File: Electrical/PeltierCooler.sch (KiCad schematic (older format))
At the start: 45 parts

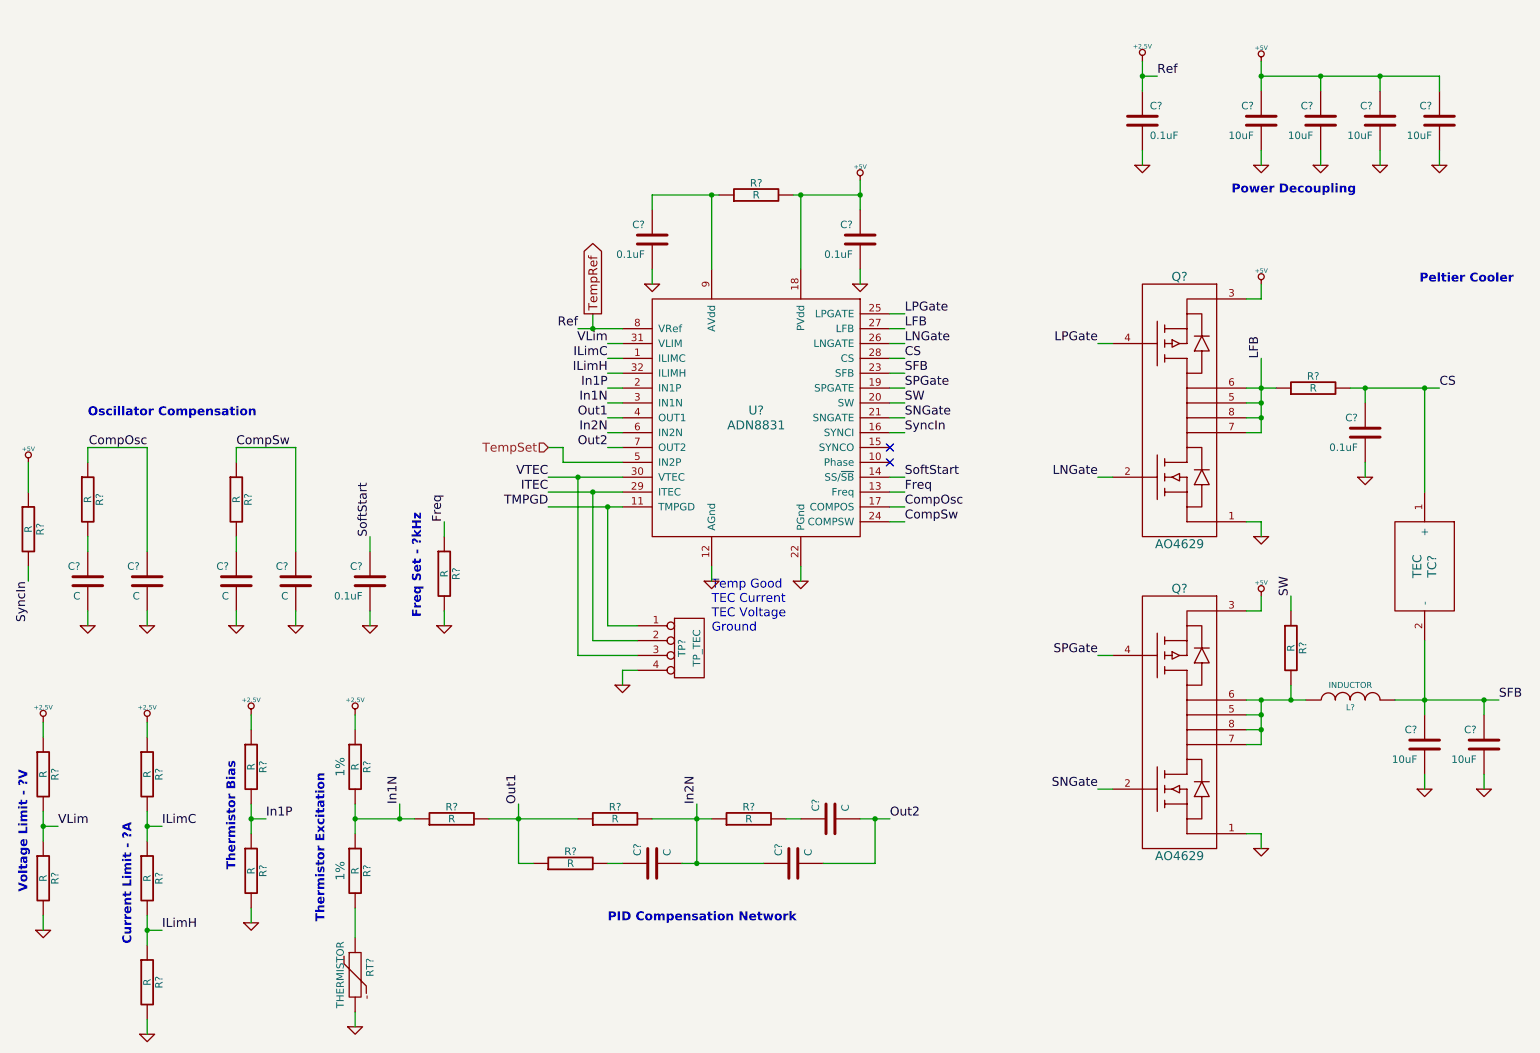
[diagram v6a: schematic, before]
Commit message: Implementing TEC controller
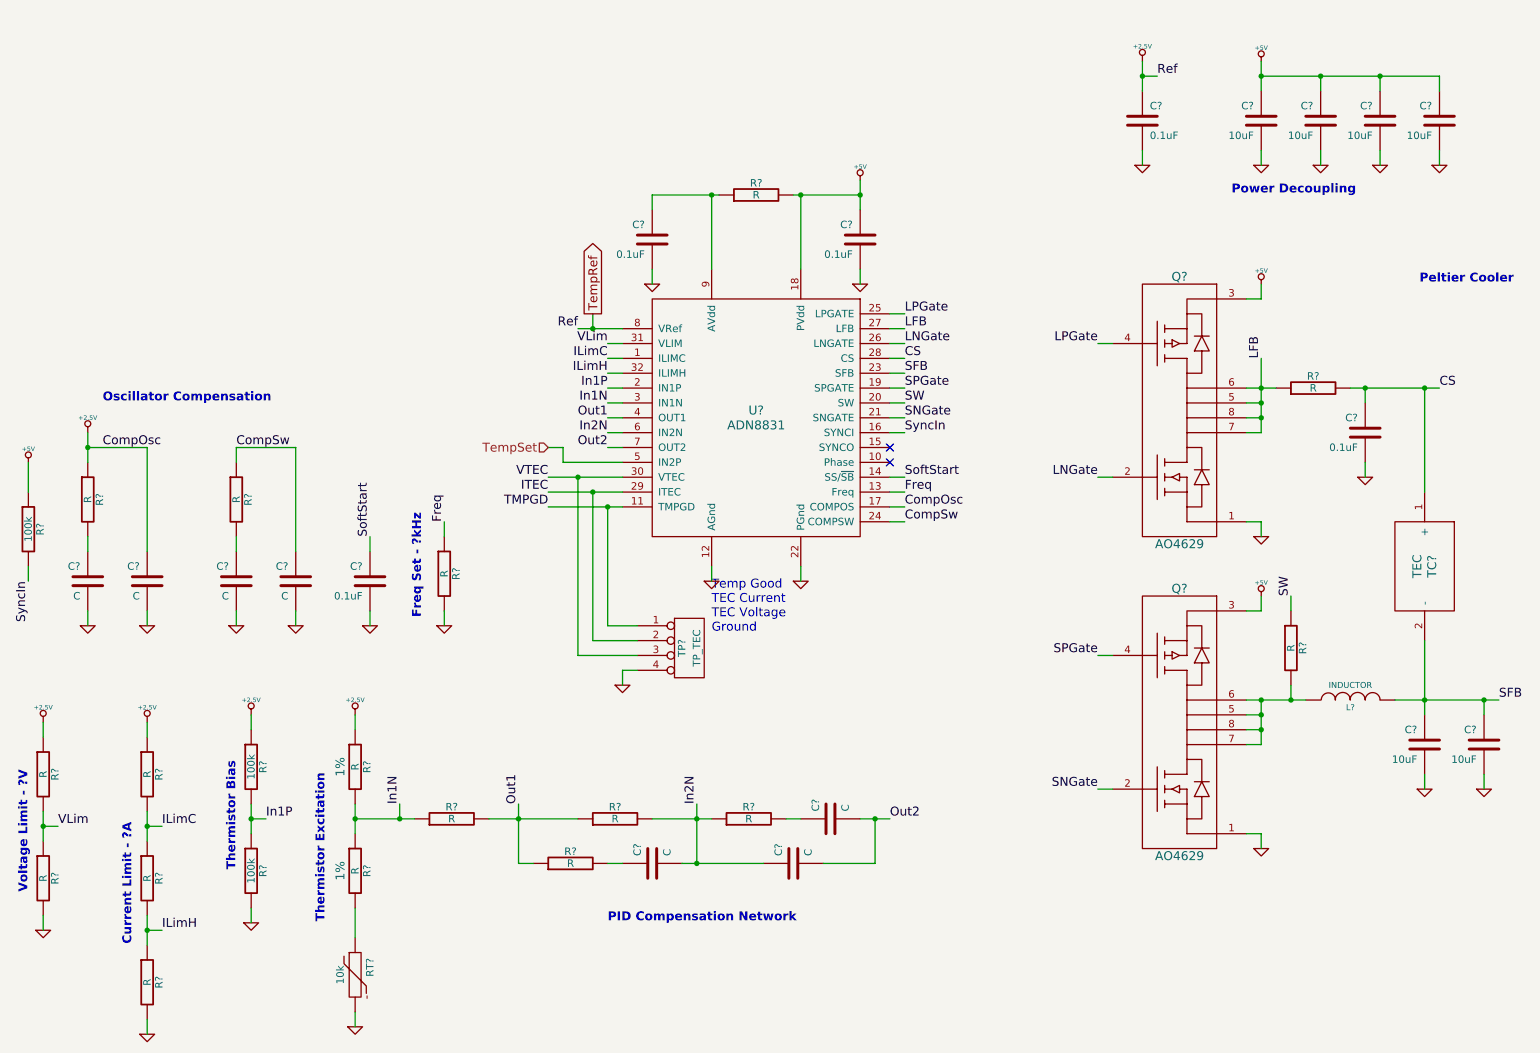
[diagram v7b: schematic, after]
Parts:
- R? (x3): value R -> 100k
- RT?: value THERMISTOR -> 10k
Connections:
- net CompOsc is gone; now on net +2.5V: C?.1, R?.1, U?.17 (COMPOS)

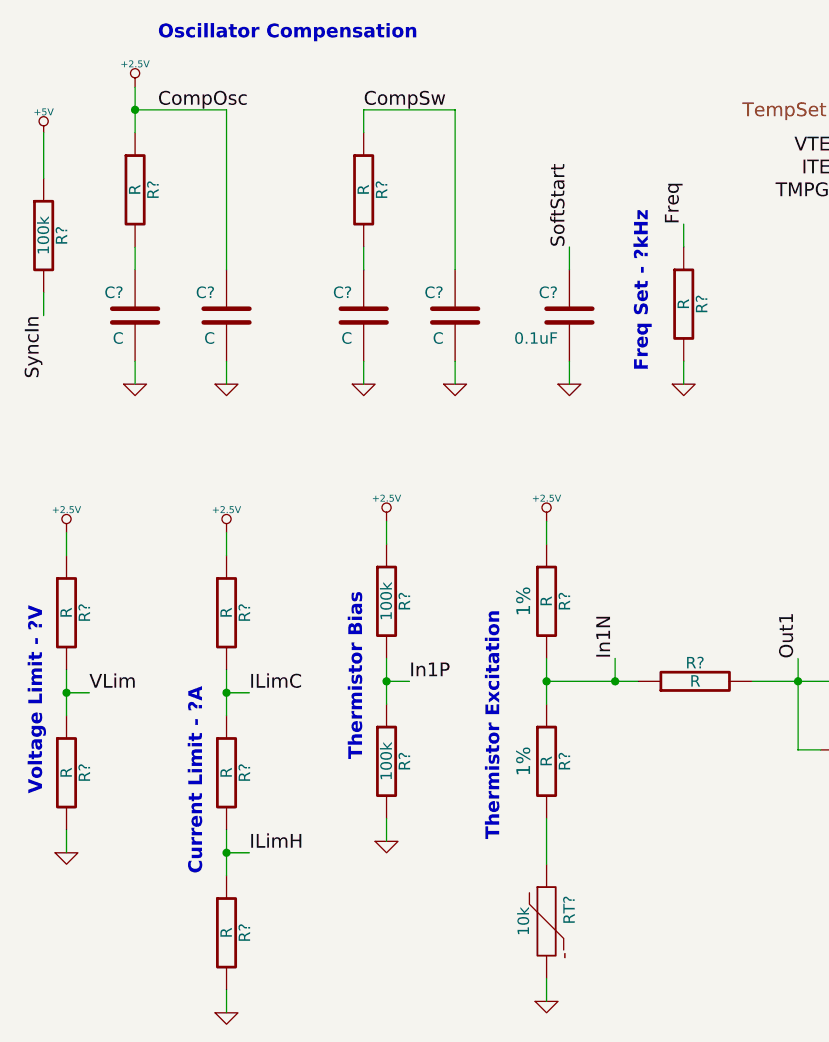
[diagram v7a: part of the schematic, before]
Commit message: Added sensors/data logger with ChipKit Max
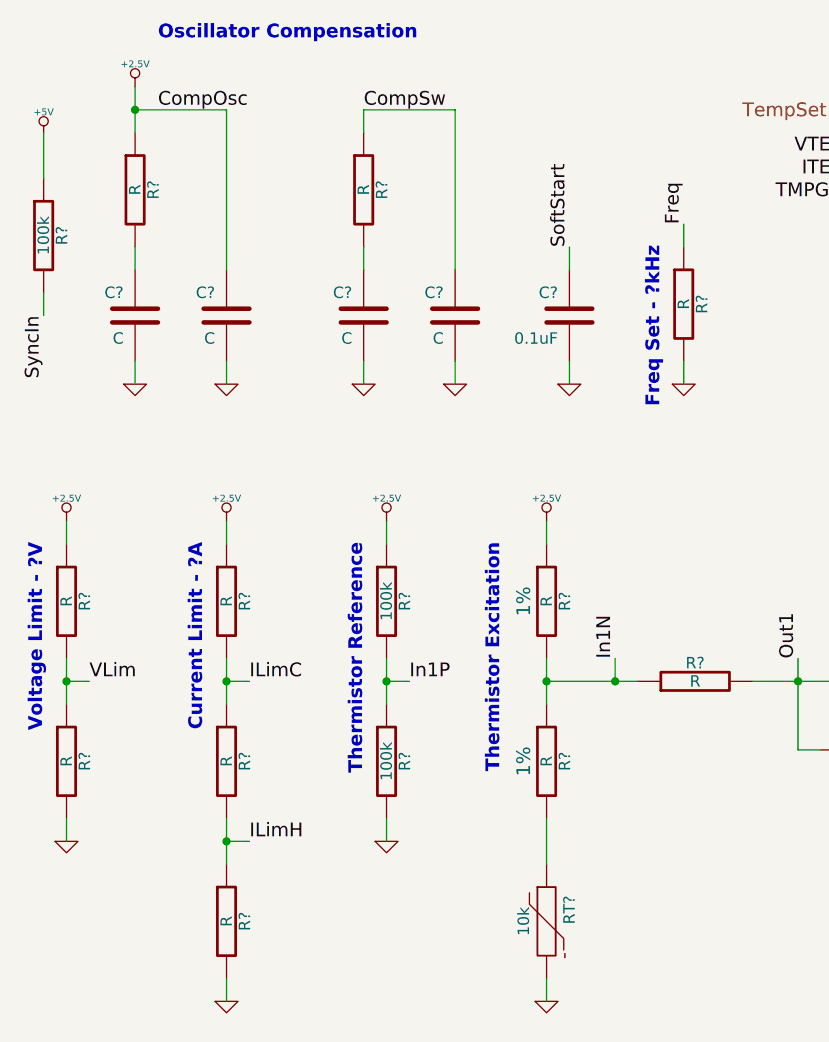
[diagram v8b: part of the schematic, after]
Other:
- note added: "Thermistor Reference"
- note removed: "Thermistor Bias"
- moved on the sheet: R?
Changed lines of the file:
@@
-EESchema Schematic File Version 2  date 4/19/2013 7:14:36 PM
+EESchema Schematic File Version 2  date 5/4/2013 6:32:29 PM
 LIBS:power
 LIBS:device
@@
 $Descr A4 11700 8267
 encoding utf-8
-Sheet 6 6
+Sheet 6 7
 Title "Cosmic Ray Detector"
-Date "20 apr 2013"
+Date "4 may 2013"
 Rev "1A"
 Comp "Ethan Harstad"
@@
 Wire Wire Line
 	2400 5300 2400 5400
-Connection ~ 1700 6750
-Wire Wire Line
-	1800 6750 1700 6750
-Wire Wire Line
-	1700 6150 1700 5950
-Wire Wire Line
-	1700 7450 1700 7350
-Wire Wire Line
-	1000 6750 1000 6650
-Wire Wire Line
-	1000 5350 1000 5450
+Connection ~ 1700 6700
+Wire Wire Line
+	1800 6700 1700 6700
+Wire Wire Line
+	1700 6100 1700 5900
+Wire Wire Line
+	1700 7400 1700 7300
+Wire Wire Line
+	1000 6700 1000 6600
+Wire Wire Line
+	1000 5300 1000 5400
 Wire Wire Line
 	4800 3000 4900 3000
@@
 Connection ~ 8400 1000
 Wire Wire Line
-	1000 5950 1000 6150
-Wire Wire Line
-	1100 6050 1000 6050
-Connection ~ 1000 6050
-Wire Wire Line
-	1700 6650 1700 6850
-Wire Wire Line
-	1700 5350 1700 5450
-Wire Wire Line
-	1800 6050 1700 6050
-Connection ~ 1700 6050
+	1000 5900 1000 6100
+Wire Wire Line
+	1100 6000 1000 6000
+Connection ~ 1000 6000
+Wire Wire Line
+	1700 6600 1700 6800
+Wire Wire Line
+	1700 5300 1700 5400
+Wire Wire Line
+	1800 6000 1700 6000
+Connection ~ 1700 6000
 Wire Wire Line
 	2400 6700 2400 6600
@@
 Text Notes 1400 3200 0    60   ~ 12
 Oscillator Compensation
-Text Notes 3550 4650 1    60   ~ 12
+Text Notes 3600 4100 3    60   ~ 12
 Freq Set - ?kHz
-Text Notes 2300 6350 1    60   ~ 12
-Thermistor Bias
-Text Notes 1600 6850 1    60   ~ 12
+Text Notes 2300 5400 3    60   ~ 12
+Thermistor Reference
+Text Notes 1600 5400 3    60   ~ 12
 Current Limit - ?A
-Text Notes 900  6500 1    60   ~ 12
+Text Notes 900  5400 3    60   ~ 12
 Voltage Limit - ?V
 $Comp
@@
 	1    0    0    -1
 $EndComp
-Text Notes 2900 6700 1    60   ~ 12
+Text Notes 2900 5400 3    60   ~ 12
 Thermistor Excitation
 Text Notes 4800 6700 0    60   ~ 12
@@
 L +2.5V #PWR?
 U 1 1 516B5589
-P 1700 5350
-F 0 "#PWR?" H 1700 5300 20  0001 C CNN
-F 1 "+2.5V" H 1700 5450 30  0000 C CNN
-	1    1700 5350
+P 1700 5300
+F 0 "#PWR?" H 1700 5250 20  0001 C CNN
+F 1 "+2.5V" H 1700 5400 30  0000 C CNN
+	1    1700 5300
 	1    0    0    -1
 $EndComp
@@
 L +2.5V #PWR?
 U 1 1 516B5586
-P 1000 5350
-F 0 "#PWR?" H 1000 5300 20  0001 C CNN
-F 1 "+2.5V" H 1000 5450 30  0000 C CNN
-	1    1000 5350
+P 1000 5300
+F 0 "#PWR?" H 1000 5250 20  0001 C CNN
+F 1 "+2.5V" H 1000 5400 30  0000 C CNN
+	1    1000 5300
 	1    0    0    -1
 $EndComp
@@
 L R R?
 U 1 1 516B54BD
-P 1000 5700
-F 0 "R?" V 1080 5700 50  0000 C CNN
-F 1 "R" V 1000 5700 50  0000 C CNN
-	1    1000 5700
+P 1000 5650
+F 0 "R?" V 1080 5650 50  0000 C CNN
+F 1 "R" V 1000 5650 50  0000 C CNN
+	1    1000 5650
 	1    0    0    -1
 $EndComp
@@
 L R R?
 U 1 1 516B54BC
-P 1000 6400
-F 0 "R?" V 1080 6400 50  0000 C CNN
-F 1 "R" V 1000 6400 50  0000 C CNN
-	1    1000 6400
+P 1000 6350
+F 0 "R?" V 1080 6350 50  0000 C CNN
+F 1 "R" V 1000 6350 50  0000 C CNN
+	1    1000 6350
 	1    0    0    -1
 $EndComp
@@
 L GND #PWR?
 U 1 1 516B54BB
-P 1000 6750
-F 0 "#PWR?" H 1000 6750 30  0001 C CNN
-F 1 "GND" H 1000 6680 30  0001 C CNN
-	1    1000 6750
-	1    0    0    -1
-$EndComp
-Text Label 1100 6050 0    60   ~ 0
+P 1000 6700
+F 0 "#PWR?" H 1000 6700 30  0001 C CNN
+F 1 "GND" H 1000 6630 30  0001 C CNN
+	1    1000 6700
+	1    0    0    -1
+$EndComp
+Text Label 1100 6000 0    60   ~ 0
 VLim
 $Comp
 L R R?
 U 1 1 516B54BA
-P 1700 5700
-F 0 "R?" V 1780 5700 50  0000 C CNN
-F 1 "R" V 1700 5700 50  0000 C CNN
-	1    1700 5700
+P 1700 5650
+F 0 "R?" V 1780 5650 50  0000 C CNN
+F 1 "R" V 1700 5650 50  0000 C CNN
+	1    1700 5650
 	1    0    0    -1
 $EndComp
@@
 L R R?
 U 1 1 516B54B9
-P 1700 6400
-F 0 "R?" V 1780 6400 50  0000 C CNN
-F 1 "R" V 1700 6400 50  0000 C CNN
-	1    1700 6400
+P 1700 6350
+F 0 "R?" V 1780 6350 50  0000 C CNN
+F 1 "R" V 1700 6350 50  0000 C CNN
+	1    1700 6350
 	1    0    0    -1
 $EndComp
@@
 L R R?
 U 1 1 516B54B8
-P 1700 7100
-F 0 "R?" V 1780 7100 50  0000 C CNN
-F 1 "R" V 1700 7100 50  0000 C CNN
-	1    1700 7100
+P 1700 7050
+F 0 "R?" V 1780 7050 50  0000 C CNN
+F 1 "R" V 1700 7050 50  0000 C CNN
+	1    1700 7050
 	1    0    0    -1
 $EndComp
@@
 L GND #PWR?
 U 1 1 516B54B7
-P 1700 7450
-F 0 "#PWR?" H 1700 7450 30  0001 C CNN
-F 1 "GND" H 1700 7380 30  0001 C CNN
-	1    1700 7450
-	1    0    0    -1
-$EndComp
-Text Label 1800 6050 0    60   ~ 0
+P 1700 7400
+F 0 "#PWR?" H 1700 7400 30  0001 C CNN
+F 1 "GND" H 1700 7330 30  0001 C CNN
+	1    1700 7400
+	1    0    0    -1
+$EndComp
+Text Label 1800 6000 0    60   ~ 0
 ILimC
-Text Label 1800 6750 0    60   ~ 0
+Text Label 1800 6700 0    60   ~ 0
 ILimH
 $Comp
